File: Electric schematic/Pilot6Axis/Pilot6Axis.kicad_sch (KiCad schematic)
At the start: 63 parts, among them IC1 ESP32-WROOM-32U, IC2 LM27313XMFX_NOPB, J1 BTN1, J10 Power switch, J11 TP4056, J12 OLED, J13 USB_C_Receptacle_USB2.0_16P, J14 BTN9, J15 BTN11, J16 BTN10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

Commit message: Update pilot PCB versin 1.0
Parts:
- removed C1: 2.2uF, Capacitor_SMD:C_0603_1608Metric, symbol Device:C
- removed C10, C8: 10uF, Resistor_SMD:R_0603_1608Metric, symbol Device:C
- removed C11, C9: 0.1uF, Resistor_SMD:R_0603_1608Metric, symbol Device:C
- removed C12, C13, C4, C5: 1nF, Capacitor_SMD:C_0603_1608Metric, symbol Device:C
- removed C14, C15: 100nF, Capacitor_SMD:C_0603_1608Metric, symbol Device:C
- removed C2: 4.7uF, Capacitor_SMD:C_0603_1608Metric, symbol Device:C
- removed C3: 220pF, Capacitor_SMD:C_0603_1608Metric, symbol Device:C
- removed C6: 10uF, Capacitor_SMD:C_0603_1608Metric, symbol Device:C
- removed C7: 10nF, Resistor_SMD:R_0603_1608Metric, symbol Device:C
- removed D1: MBR0520, Diode_SMD:D_0603_1608Metric, symbol Device:D_Schottky
- removed D2, D3: LED, LED_SMD:LED_0603_1608Metric, symbol Device:LED
- removed IC1: ESP32-WROOM-32U, ESP32-WROOM-32U:ESP32WROOM32D, symbol ESP32-WROOM-32U:ESP32-WROOM-32U
- removed IC2: LM27313XMFX_NOPB, KLM27313XMF_NOPB:SOT95P280X145-5N, symbol LM27313XMFX_NOPB:LM27313XMFX_NOPB
- removed J1: BTN1, molex-2pin:HDRV2W64P254_1X2_580X508X1170P, symbol molex-2pin:22-27-2021
- removed J10: Power switch, molex-2pin:HDRV2W64P254_1X2_580X508X1170P, symbol molex-2pin:22-27-2021
- removed J11: TP4056, TP4056:SOIC127P600X175-9N, symbol TP4056:TP4056
- removed J12: OLED, Connector_PinSocket_2.54mm:PinSocket_2x02_P2.54mm_Vertical, symbol molex-4pin:22232041
- removed J13: USB_C_Receptacle_USB2.0_16P, Connector_USB:USB_C_Receptacle_HCTL_HC-TYPE-C-16P-01A, symbol Connector:USB_C_Receptacle_USB2.0_16P
- removed J14: BTN9, molex-2pin:HDRV2W64P254_1X2_580X508X1170P, symbol molex-2pin:22-27-2021
- removed J15: BTN11, molex-2pin:HDRV2W64P254_1X2_580X508X1170P, symbol molex-2pin:22-27-2021
- removed J16: BTN10, molex-2pin:HDRV2W64P254_1X2_580X508X1170P, symbol molex-2pin:22-27-2021
- removed J2: BTN2, molex-2pin:HDRV2W64P254_1X2_580X508X1170P, symbol molex-2pin:22-27-2021
- removed J3: BTN3, molex-2pin:HDRV2W64P254_1X2_580X508X1170P, symbol molex-2pin:22-27-2021
- removed J4: BTN4, molex-2pin:HDRV2W64P254_1X2_580X508X1170P, symbol molex-2pin:22-27-2021
- removed J5: BTN5, molex-2pin:HDRV2W64P254_1X2_580X508X1170P, symbol molex-2pin:22-27-2021
- removed J6: BTN6, molex-2pin:HDRV2W64P254_1X2_580X508X1170P, symbol molex-2pin:22-27-2021
- removed J7: BTN7, molex-2pin:HDRV2W64P254_1X2_580X508X1170P, symbol molex-2pin:22-27-2021
- removed J8: BTN8, molex-2pin:HDRV2W64P254_1X2_580X508X1170P, symbol molex-2pin:22-27-2021
- removed J9: BAT, molex-2pin:HDRV2W64P254_1X2_580X508X1170P, symbol molex-2pin:22-27-2021
- removed L1: 10uH, Inductor_SMD:L_APV_ANR4010, symbol Device:L
- removed Q1, Q2: Q_NPN_EBC, S8050:SOT95P240X115-3N, symbol Device:Q_NPN_EBC
- removed R1: 40.5k, Resistor_SMD:R_0603_1608Metric, symbol Device:R
- removed R10, R9: 5k1, Resistor_SMD:R_0603_1608Metric, symbol Device:R
- removed R11: 33k, Resistor_SMD:R_0603_1608Metric, symbol Device:R
- removed R12, R5, R6: 1k, Resistor_SMD:R_0603_1608Metric, symbol Device:R
- removed R15, R18, R19: 470R, Resistor_SMD:R_0603_1608Metric, symbol Device:R
- removed R16, R17, R2: 13.3k, Resistor_SMD:R_0603_1608Metric, symbol Device:R
- removed R3: 1.2k, Resistor_SMD:R_0603_1608Metric, symbol Device:R
- removed R4: 0.5, Resistor_SMD:R_0603_1608Metric, symbol Device:R
- removed R7, R8: 22R, Resistor_SMD:R_0603_1608Metric, symbol Device:R
- removed SW1, SW2: SW_Push, TS-1088R-02026:TS1088R02026, symbol Switch:SW_Push
- removed U1: JOYSTICK1, Connector_PinSocket_2.54mm:PinSocket_2x03_P2.54mm_Vertical, symbol molex-6pin:22-27-2061
- removed U2: JOYSTICK2, Connector_PinSocket_2.54mm:PinSocket_2x03_P2.54mm_Vertical, symbol molex-6pin:22-27-2061
- removed U3: AMS1117-3.3, Package_TO_SOT_SMD:SOT-223-3_TabPin2, symbol Regulator_Linear:AMS1117-3.3
- removed U4: USBLC6-2SC6, Package_TO_SOT_SMD:SOT-23-6, symbol Power_Protection:USBLC6-2SC6
- removed U5: CP2102N-Axx-xQFN28, Package_DFN_QFN:QFN-28-1EP_5x5mm_P0.5mm_EP3.35x3.35mm, symbol Interface_USB:CP2102N-Axx-xQFN28
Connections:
- no-connect marks 2 -> 0
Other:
- added sheet CHARGER (CHARGER.kicad_sch)
- added sheet MCU (MCU.kicad_sch)
- added sheet Power (Power.kicad_sch)
- added sheet USB (USB.kicad_sch)
- note removed: "Buttons input"
- note removed: "Joystick input"
- note removed: "OLED connector"
- note removed: "Power supply"
- note removed: "USB C"

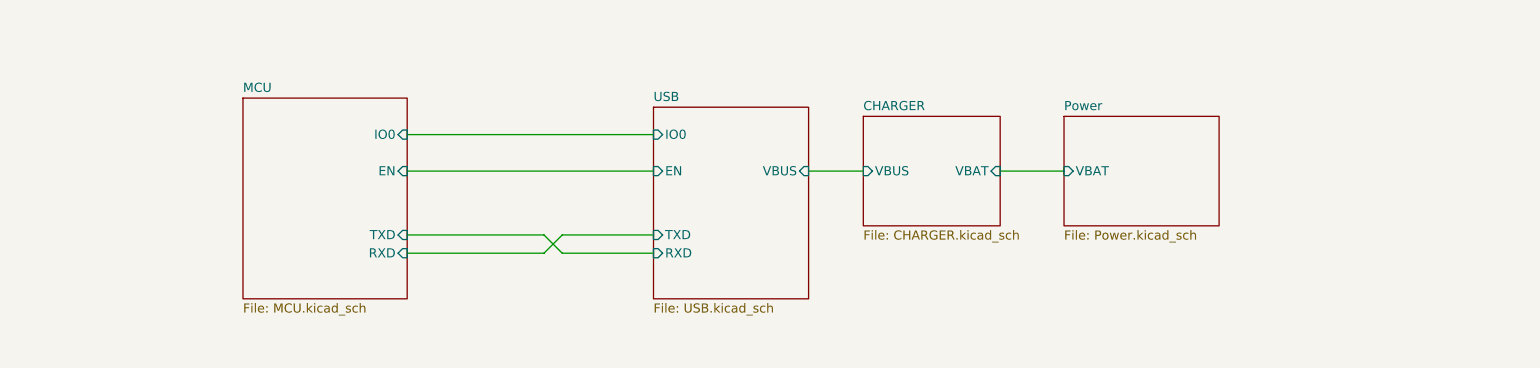
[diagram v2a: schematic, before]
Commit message: upgrade board to use USB BD for power delivery and addded SPI screen conector
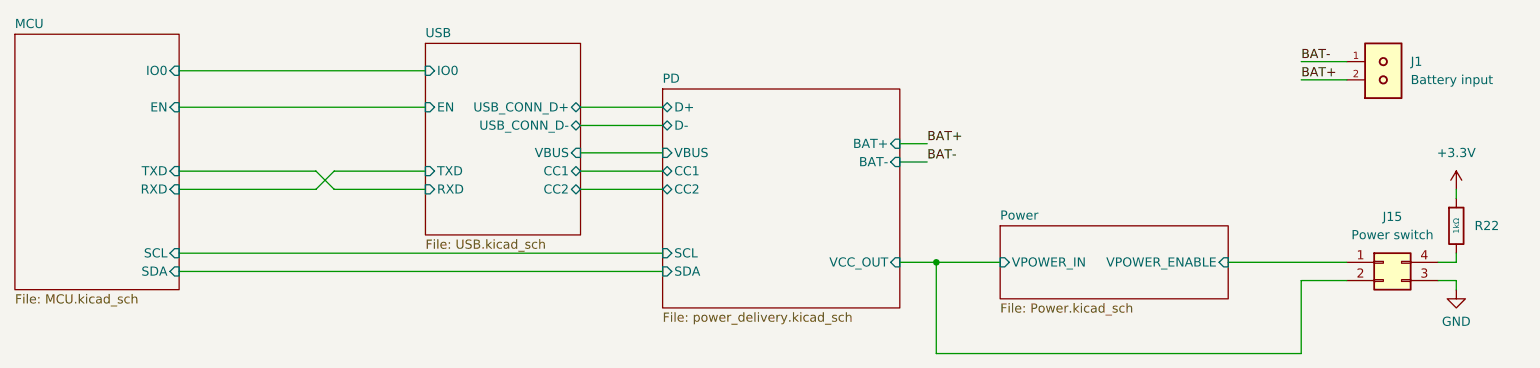
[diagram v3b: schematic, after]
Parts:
- added J1: Battery input, Connector_Molex:Molex_KK-254_AE-6410-02A_1x02_P2.54mm_Vertical, symbol molex-2pin:22-27-2021
- added J15: Power switch, Connector_Molex:Molex_KK-254_AE-6410-04A_1x04_P2.54mm_Vertical, symbol Connector_Generic:Conn_02x02_Counter_Clockwise
- added R22: 1kΩ, PCM_JLCPCB:R_0603, symbol PCM_JLCPCB-Resistors:0603,1kΩ
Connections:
- new net: J15.4 (Pin_4), R22.2
- new net +3.3V: R22.1
- new net BAT+: J1.2
- new net BAT-: J1.1
- new net GND: J15.3 (Pin_3)
- new net PD/VCC_OUT: J15.2 (Pin_2)
- new net Power/VPOWER_ENABLE: J15.1 (Pin_1)
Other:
- removed sheet CHARGER
- added sheet PD (power_delivery.kicad_sch)
- sheet MCU ports: added SCL, SDA; removed none
- sheet Power ports: added VPOWER_ENABLE, VPOWER_IN; removed VBAT
- sheet USB ports: added CC1, CC2, USB_CONN_D+, USB_CONN_D-; removed none

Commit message: fixed leyout
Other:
- sheet PD ports: added none; removed D+, D-
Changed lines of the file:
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@@
-	(wire
-		(pts
-			(xy 134.62 74.93) (xy 146.05 74.93)
-		)
-		(stroke
-			(width 0)
-			(type default)
-		)
-	)
 	(wire
 		(pts
@@
 		(pts
 			(xy 184.15 109.22) (xy 234.95 109.22)
-		)
-		(stroke
-			(width 0)
-			(type default)
-		)
-	)
-	(wire
-		(pts
-			(xy 134.62 77.47) (xy 146.05 77.47)
 		)
 		(stroke
@@
 			)
 		)
-		(pin "D+" bidirectional
-			(at 146.05 74.93 180)
-			(effects
-				(font
-					(size 1.27 1.27)
-				)
-				(justify left)
-			)
-		)
-		(pin "D-" bidirectional
-			(at 146.05 77.47 180)
-			(effects
-				(font
-					(size 1.27 1.27)
-				)
-				(justify left)
-			)
-		)
